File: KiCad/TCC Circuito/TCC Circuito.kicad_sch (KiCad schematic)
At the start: 6 parts, among them J1 Sensor HALL, J2 Rasp pico, U1 TL071, U2 INA333xxDGK, U3 ADS1115IDGS

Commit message: dois buffers
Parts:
- removed U2: INA333xxDGK, Package_SO:VSSOP-8_3x3mm_P0.65mm, symbol Amplifier_Instrumentation:INA333xxDGK
- removed U3: ADS1115IDGS, Package_SO:TSSOP-10_3x3mm_P0.5mm, symbol Analog_ADC:ADS1115IDGS
- added U2: TL071, symbol Amplifier_Operational:TL071
- added U3: INA128, symbol Amplifier_Instrumentation:INA128
- added U4: ADS1115IDGS, Package_SO:TSSOP-10_3x3mm_P0.5mm, symbol Analog_ADC:ADS1115IDGS
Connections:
- net +5V: now also U2.7 (V+), U3.7 (V+), U4.8 (VDD)
- net -5V: now also U2.4 (V-), U3.4 (V-)
- net GND: now also U3.5 (Ref), U4.3 (GND)
- net at J1.2 (Pin_2): now also U2.3 (+)
- net at U1.2 (-), U1.6: now also U3.3 (+)
- net at U1.1 (NULL): no longer RV1.3
- net at U1.5 (NULL): no longer RV1.1
- net at J2.4 (Pin_4): now also U4.1 (ADDR)
- net at J2.2 (Pin_2): now also U4.10 (SCL)
- net at J2.1 (Pin_1): now also U4.2 (ALERT/RDY)
- net at J2.3 (Pin_3): now also U4.9 (SDA)
- new net: RV1.3, U2.1 (NULL)
- new net: U2.2 (-), U2.6, U3.2 (-)
- new net: RV1.1, U2.5 (NULL)
- new net: U3.6, U4.4 (AIN0)
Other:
- moved on the sheet: J1

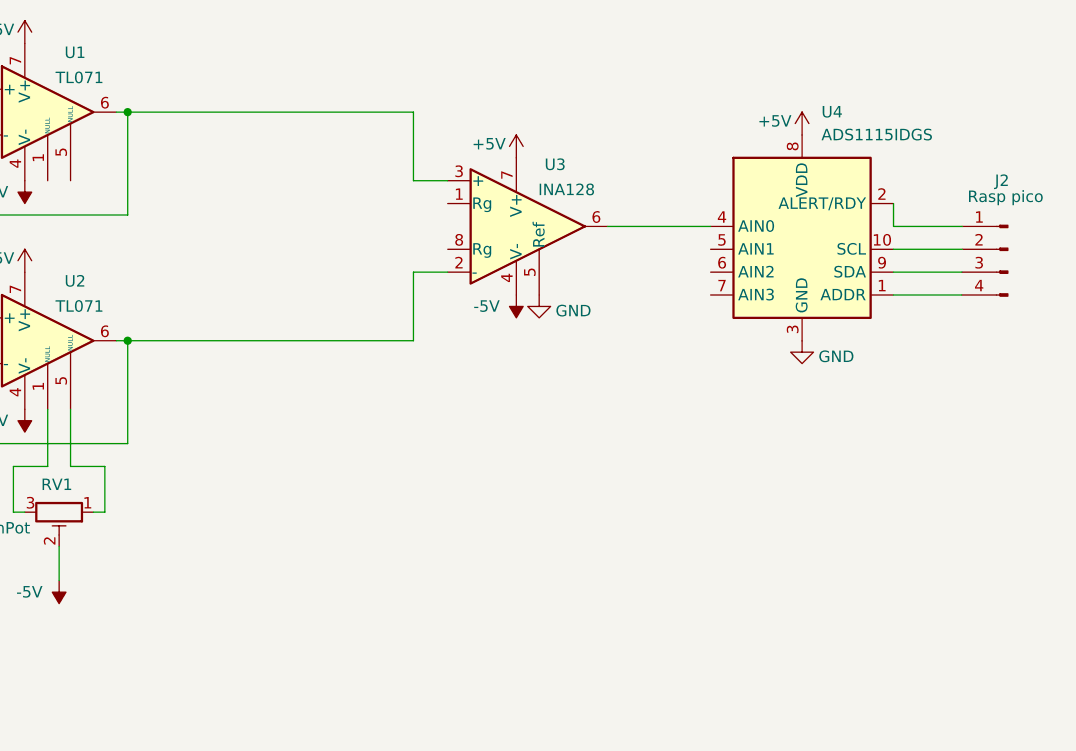
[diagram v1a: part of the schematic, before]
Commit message: ina122 e reles
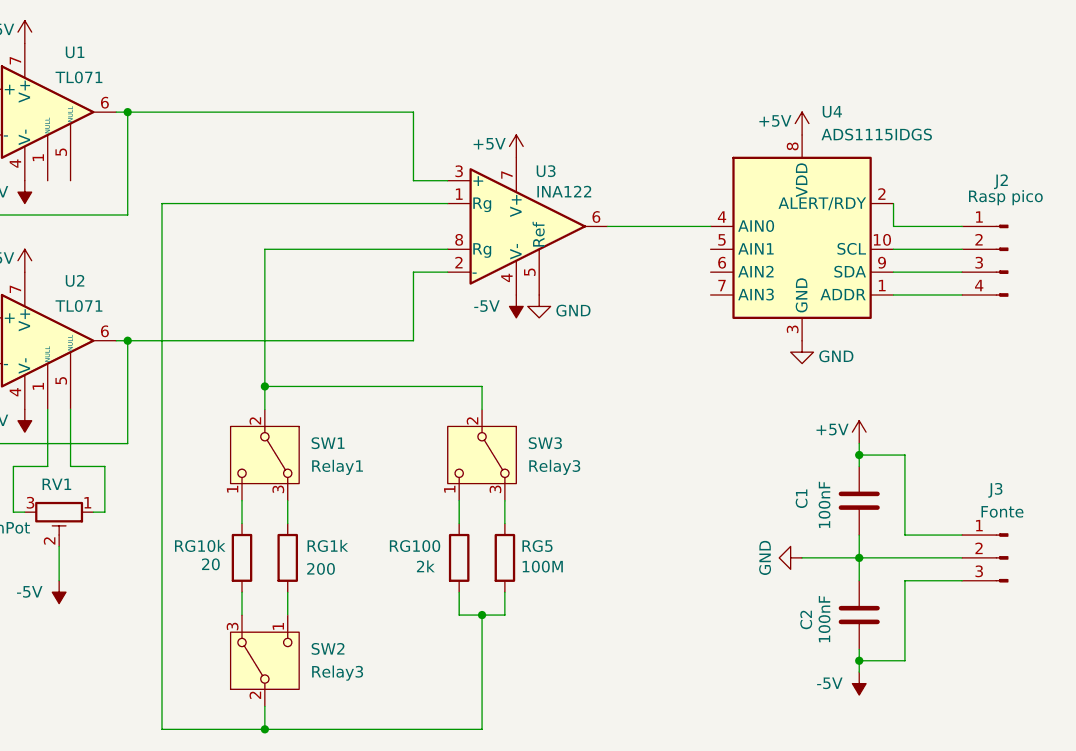
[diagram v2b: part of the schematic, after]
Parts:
- added C1, C2: 100nF, symbol Device:C
- added J3: Fonte, symbol Connector:Conn_01x03_Pin
- added RG100: 2k, symbol Device:R
- added RG10k: 20, symbol Device:R
- added RG1k: 200, symbol Device:R
- added RG5: 100M, symbol Device:R
- added SW1: Relay1, Button_Switch_SMD:Nidec_Copal_CAS-120A, symbol Switch:SW_Nidec_CAS-120A1
- added SW2, SW3: Relay3, Button_Switch_SMD:Nidec_Copal_CAS-120A, symbol Switch:SW_Nidec_CAS-120A1
- U3: value INA128 -> INA122
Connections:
- net +5V: now also C1.1, J3.1 (Pin_1)
- net -5V: now also C2.2, J3.3 (Pin_3)
- net GND: now also C1.2, C2.1, J3.2 (Pin_2)
- net at U3.1 (Rg): now also RG100.2, RG5.2, SW2.2 (B)
- net at U3.8 (Rg): now also SW1.2 (B), SW3.2 (B)
- new net: RG10k.1, SW1.1 (C)
- new net: RG1k.1, SW1.3 (A)
- new net: RG5.1, SW3.3 (A)
- new net: RG1k.2, SW2.1 (C)
- new net: RG10k.2, SW2.3 (A)
- new net: RG100.1, SW3.1 (C)

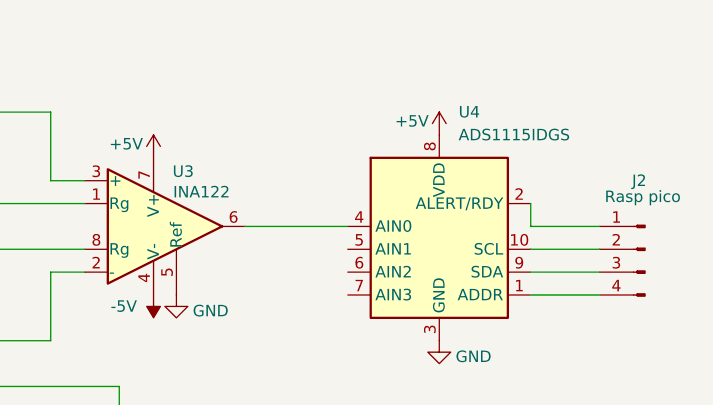
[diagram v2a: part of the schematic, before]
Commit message: codigo com ADC funcionando bem
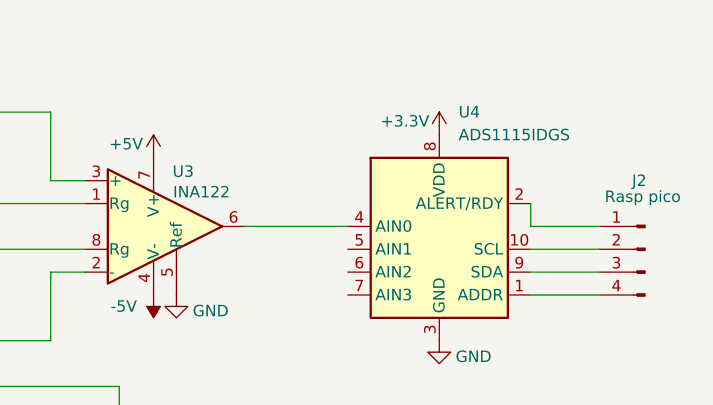
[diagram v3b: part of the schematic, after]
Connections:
- net +5V: no longer U4.8 (VDD)
- new net +3.3V: U4.8 (VDD)
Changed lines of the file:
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@@
+	)
+	(symbol
+		(lib_id "power:+3.3V")
+		(at 196.85 74.93 0)
+		(unit 1)
+		(exclude_from_sim no)
+		(in_bom yes)
+		(on_board yes)
+		(dnp no)
+		(property "Reference" "#PWR04"
+			(at 196.85 78.74 0)
+			(effects
+				(font
+					(size 1.27 1.27)
+				)
+				(hide yes)
+			)
+		)
+		(property "Value" "+3.3V"
+			(at 193.04 73.406 0)
+			(effects
+				(font
+					(size 1.27 1.27)
+				)
+			)
+		)
+		(property "Footprint" ""
+			(at 196.85 74.93 0)
+			(effects
+				(font
+					(size 1.27 1.27)
+				)
+				(hide yes)
+			)
+		)
+		(property "Datasheet" ""
+			(at 196.85 74.93 0)
+			(effects
+				(font
+					(size 1.27 1.27)
+				)
+				(hide yes)
+			)
+		)
+		(property "Description" "Power symbol creates a global label with name \"+3.3V\""
+			(at 196.85 74.93 0)
+			(effects
+				(font
+					(size 1.27 1.27)
+				)
+				(hide yes)
+			)
+		)
+		(pin "1"
+		)
+		(instances
+			(project ""
+				(path "/47032d33-7038-4871-a5b9-c8b9c3fb37c1"
+					(reference "#PWR04")
+					(unit 1)
+				)
+			)
+		)
 	)
 	(symbol
@@
 					(unit 1)
 				)
-			)
-		)
-	)
-	(symbol
-		(lib_id "power:+5V")
-		(at 196.85 74.93 0)
-		(unit 1)
-		(exclude_from_sim no)
-		(in_bom yes)
-		(on_board yes)
-		(dnp no)
-		(property "Reference" "#PWR012"
-			(at 196.85 78.74 0)
-			(effects
-				(font
-					(size 1.27 1.27)
-				)
-				(hide yes)
-			)
-		)
-		(property "Value" "+5V"
-			(at 193.802 73.406 0)
-			(effects
-				(font
-					(size 1.27 1.27)
-				)
-			)
-		)
-		(property "Footprint" ""
-			(at 196.85 74.93 0)
-			(effects
-				(font
-					(size 1.27 1.27)
-				)
-				(hide yes)
-			)
-		)
-		(property "Datasheet" ""
-			(at 196.85 74.93 0)
-			(effects
-				(font
-					(size 1.27 1.27)
-				)
-				(hide yes)
-			)
-		)
-		(property "Description" "Power symbol creates a global label with name \"+5V\""
-			(at 196.85 74.93 0)
-			(effects
-				(font
-					(size 1.27 1.27)
-				)
-				(hide yes)
-			)
-		)
-		(pin "1"
-		)
-		(instances
-			(project "TCC Circuito"
-				(path "/47032d33-7038-4871-a5b9-c8b9c3fb37c1"
-					(reference "#PWR012")
-					(unit 1)
-				)

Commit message: kicad com filtros
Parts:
- added CF+, Cf-: 100μF, symbol Device:C
- added Cfout: 1μF, symbol Device:C
- added RG100: 2k, symbol Device:R
- added Rf+, Rf-: 10k, symbol Device:R
- added Rfout: 1k, symbol Device:R
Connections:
- net GND: now also CF+.2, Cf-.2, Cfout.2
- net at SW1.2 (B), SW3.2 (B): no longer U3.8 (Rg)
- net at U1.2 (-), U1.6: now also Rf+.1; no longer U3.3 (+)
- net at RG100.2, RG5.2, SW2.2 (B): no longer U3.1 (Rg)
- net at U2.2 (-), U2.6: now also Rf-.1; no longer U3.2 (-)
- net at U3.6: now also Rfout.1; no longer U4.4 (AIN0)
- new net: CF+.1, Rf+.2, U3.3 (+)
- new net: Cf-.1, Rf-.2, U3.2 (-)
- new net: RG100.1, U3.1 (Rg)
- new net: RG100.2, U3.8 (Rg)
- new net: Cfout.1, Rfout.2, U4.4 (AIN0)
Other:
- moved on the sheet: C1, C2, J1, J2, J3, RG100, RG10k, RG1k, RG5, SW1, SW2, SW3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
